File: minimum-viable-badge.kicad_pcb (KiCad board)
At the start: 2 copper layers, 120 x 64 mm, 67 parts, among them J101 EDGE_CONNECTOR, P101 USB, P102 BATTERY, P103 POT_LONG, P104 BUTTON_A, P105 BUTTON_B, P106 POT_SHORT, P107 MECH, P108 MECH, P109 MECH, P301 eInk, Q101 S8050, Q102 S8050, Q201 FDN340P, Q301 IRLML0030TRPBF, SW101 PRGM, SW102 RESET, SW201 ON|OFF, U101 ESP32-WROOM, U102 CP2102, U201 MCP73831, U202 NCP5501

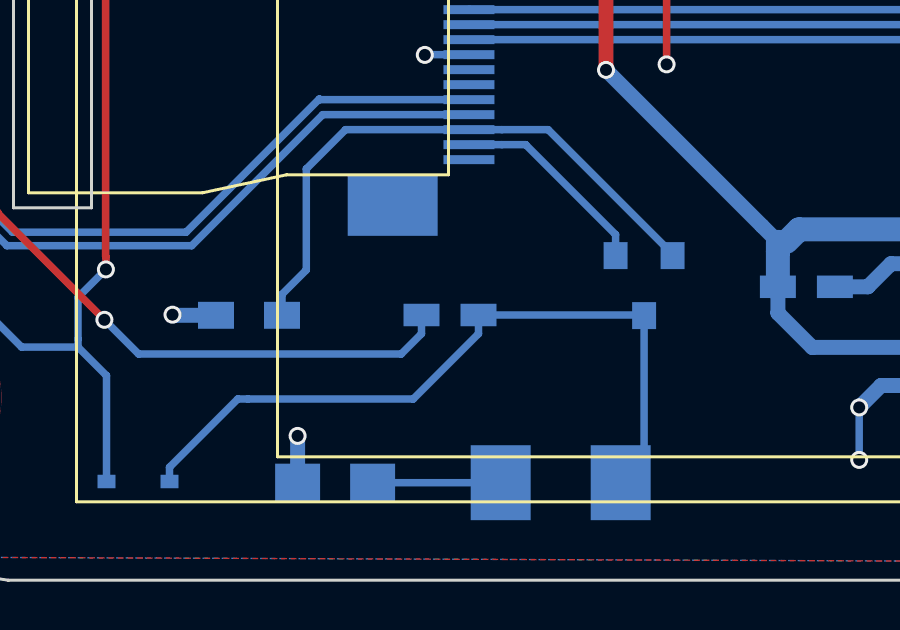
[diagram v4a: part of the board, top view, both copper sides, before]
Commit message: Swap C307 0603->0805
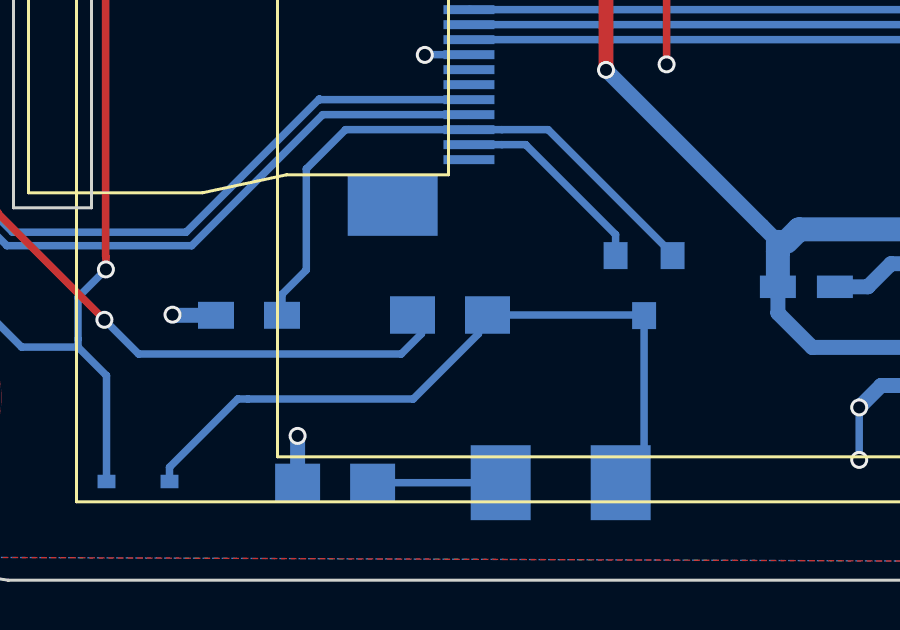
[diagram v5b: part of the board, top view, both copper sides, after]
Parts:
- C306: footprint Capacitors_SMD:C_0603_HandSoldering -> Capacitors_SMD:C_0805_HandSoldering
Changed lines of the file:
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@@
   )
   (setup
-    (last_trace_width 0.5)
+    (last_trace_width 0.25)
     (user_trace_width 0.25)
     (user_trace_width 0.5)
@@
     )
   )
-  (module Capacitors_SMD:C_0603_HandSoldering (layer B.Cu)
-    (at 44.28 73.35483 180)
-    (descr "Capacitor SMD 0603, hand soldering")
-    (tags "capacitor 0603")
-    (attr smd)
-    (fp_text reference C306 (at -0.05 -1.36 180) (layer B.SilkS)
-      (effects (font (size 1 1) (thickness 0.15)) (justify mirror))
-    )
-    (fp_text value "4.7uF 50V" (at 0 1.32 180) (layer B.Fab)
-      (effects (font (size 1 1) (thickness 0.15)) (justify mirror))
-    )
-    (fp_text user %R (at -0.05 -1.38 180) (layer B.Fab)
-      (effects (font (size 1 1) (thickness 0.15)) (justify mirror))
-    )
-    (fp_line (start -0.8 -0.4) (end -0.8 0.4) (layer B.Fab) (width 0.1))
-    (fp_line (start 0.8 -0.4) (end -0.8 -0.4) (layer B.Fab) (width 0.1))
-    (fp_line (start 0.8 0.4) (end 0.8 -0.4) (layer B.Fab) (width 0.1))
-    (fp_line (start -0.8 0.4) (end 0.8 0.4) (layer B.Fab) (width 0.1))
-    (fp_line (start -0.35 0.6) (end 0.35 0.6) (layer B.SilkS) (width 0.12))
-    (fp_line (start 0.35 -0.6) (end -0.35 -0.6) (layer B.SilkS) (width 0.12))
-    (fp_line (start -1.8 0.65) (end 1.8 0.65) (layer B.CrtYd) (width 0.05))
-    (fp_line (start -1.8 0.65) (end -1.8 -0.65) (layer B.CrtYd) (width 0.05))
-    (fp_line (start 1.8 -0.65) (end 1.8 0.65) (layer B.CrtYd) (width 0.05))
-    (fp_line (start 1.8 -0.65) (end -1.8 -0.65) (layer B.CrtYd) (width 0.05))
-    (pad 1 smd rect (at -0.95 0 180) (size 1.2 0.75) (layers B.Cu B.Paste B.Mask)
-      (net 36 "Net-(C306-Pad1)"))
-    (pad 2 smd rect (at 0.95 0 180) (size 1.2 0.75) (layers B.Cu B.Paste B.Mask)
-      (net 37 "Net-(C306-Pad2)"))
-    (model Capacitors_SMD.3dshapes/C_0603.wrl
-      (at (xyz 0 0 0))
-      (scale (xyz 1 1 1))
-      (rotate (xyz 0 0 0))
-    )
-  )
   (module Capacitors_SMD:C_0805_HandSoldering (layer B.Cu)
     (at 40.45 78.93483 180)
@@
       (at (xyz 0 0 0))
       (scale (xyz 1 1 1))
+      (rotate (xyz 0 0 0))
+    )
+  )
+  (module Capacitors_SMD:C_0805_HandSoldering (layer B.Cu)
+    (at 44.28 73.35483 180)
+    (descr "Capacitor SMD 0805, hand soldering")
+    (tags "capacitor 0805")
+    (attr smd)
+    (fp_text reference C306 (at 0 1.75 180) (layer B.SilkS)
+      (effects (font (size 1 1) (thickness 0.15)) (justify mirror))
+    )
+    (fp_text value "4.7uF 50V" (at 0 -1.75 180) (layer B.Fab)
+      (effects (font (size 1 1) (thickness 0.15)) (justify mirror))
+    )
+    (fp_text user %R (at 0 1.75 180) (layer B.Fab)
+      (effects (font (size 1 1) (thickness 0.15)) (justify mirror))
+    )
+    (fp_line (start -1 -0.62) (end -1 0.62) (layer B.Fab) (width 0.1))
+    (fp_line (start 1 -0.62) (end -1 -0.62) (layer B.Fab) (width 0.1))
+    (fp_line (start 1 0.62) (end 1 -0.62) (layer B.Fab) (width 0.1))
+    (fp_line (start -1 0.62) (end 1 0.62) (layer B.Fab) (width 0.1))
+    (fp_line (start 0.5 0.85) (end -0.5 0.85) (layer B.SilkS) (width 0.12))
+    (fp_line (start -0.5 -0.85) (end 0.5 -0.85) (layer B.SilkS) (width 0.12))
+    (fp_line (start -2.25 0.88) (end 2.25 0.88) (layer B.CrtYd) (width 0.05))
+    (fp_line (start -2.25 0.88) (end -2.25 -0.87) (layer B.CrtYd) (width 0.05))
+    (fp_line (start 2.25 -0.87) (end 2.25 0.88) (layer B.CrtYd) (width 0.05))
+    (fp_line (start 2.25 -0.87) (end -2.25 -0.87) (layer B.CrtYd) (width 0.05))
+    (pad 1 smd rect (at -1.25 0 180) (size 1.5 1.25) (layers B.Cu B.Paste B.Mask)
+      (net 36 "Net-(C306-Pad1)"))
+    (pad 2 smd rect (at 1.25 0 180) (size 1.5 1.25) (layers B.Cu B.Paste B.Mask)
+      (net 37 "Net-(C306-Pad2)"))
+    (model Capacitors_SMD.3dshapes/C_0805.wrl
+      (at (xyz 0 0 0))
+      (scale (xyz 1 1 1))

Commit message: Rename power switch SK12D07VG5 -> SK12D07VG3
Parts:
- SW201: footprint libs:SK12D07VG5 -> libs:SK12D07VG3
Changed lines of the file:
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@@
       (net 29 "Net-(C102-Pad1)"))
   )
-  (module libs:SK12D07VG5 (layer B.Cu)
+  (module libs:SK12D07VG3 (layer B.Cu)
     (at 81.68 78.13483)
     (fp_text reference SW201 (at 1.24 1.56) (layer B.SilkS)

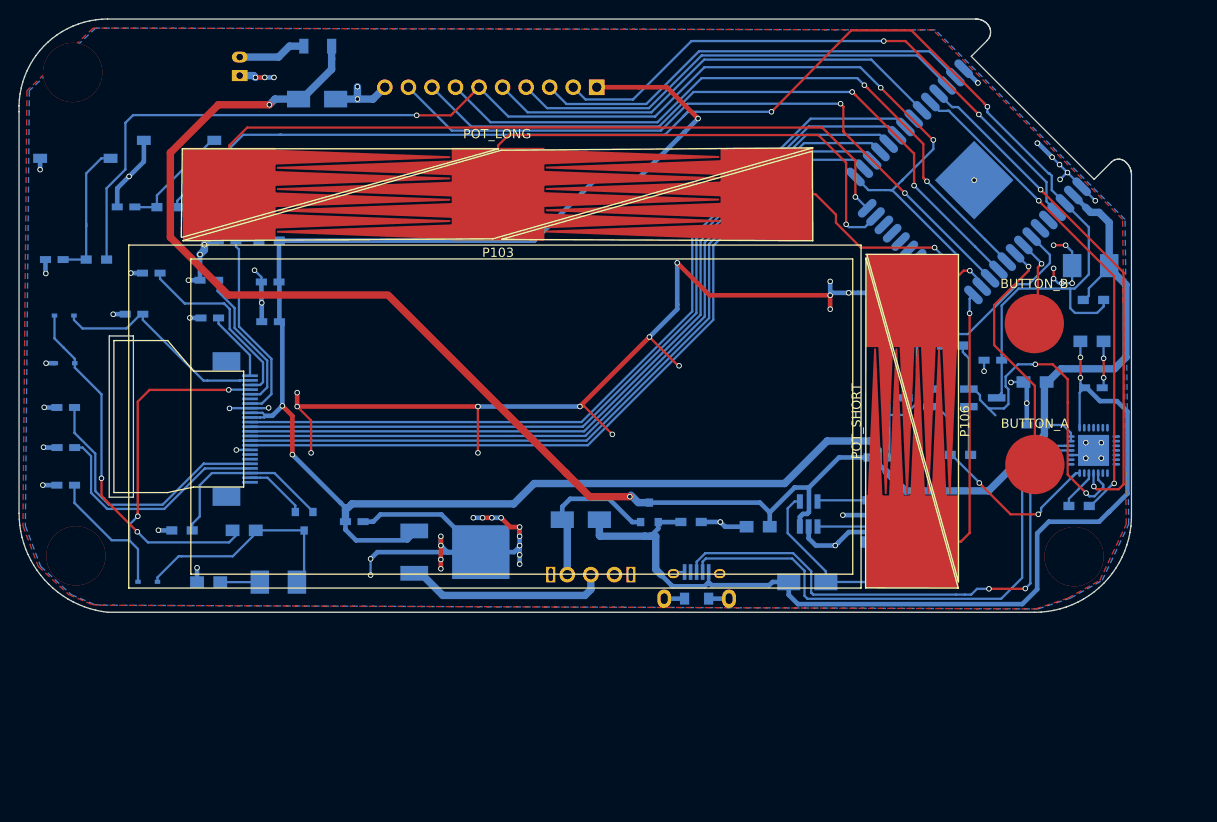
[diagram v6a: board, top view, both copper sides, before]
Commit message: Added edge connector and button silkscreen
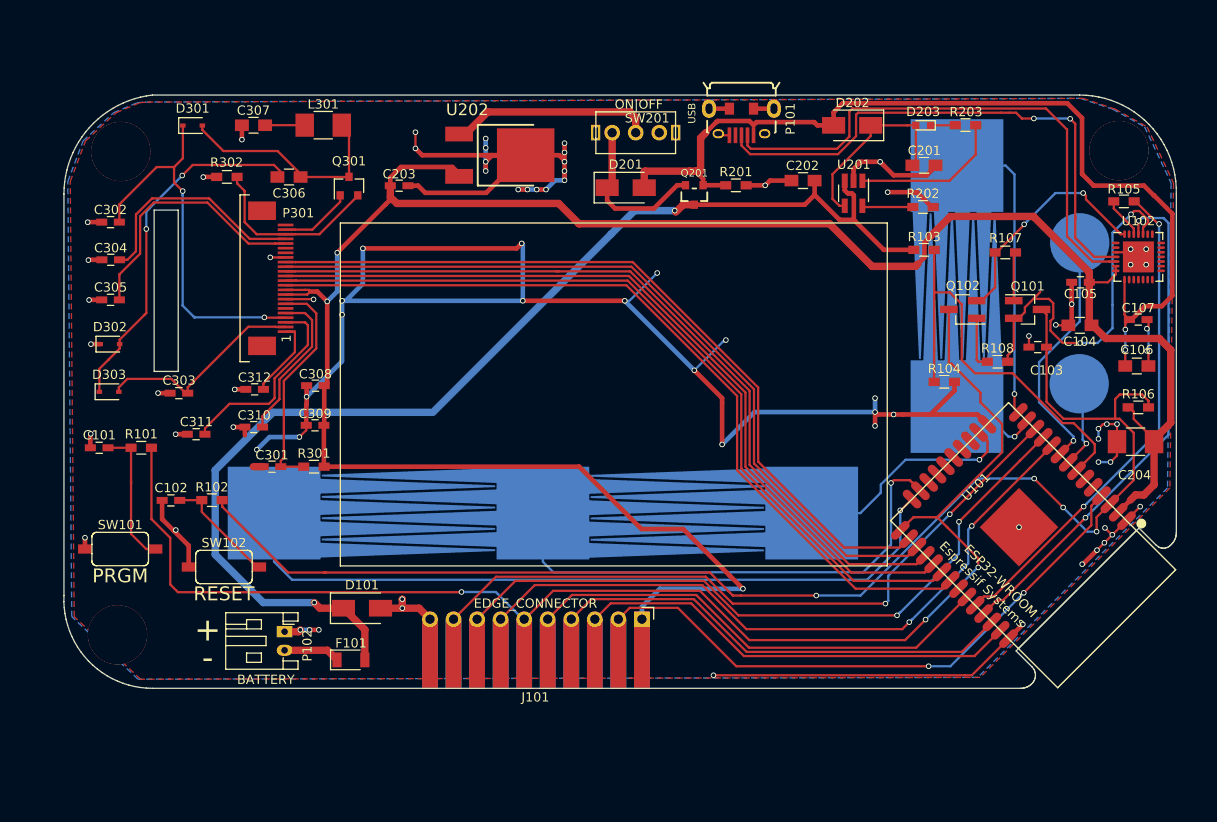
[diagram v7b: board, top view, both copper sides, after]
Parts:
- C101, C102, C103, C104, C105, C106, C107, C201, C202, C203, C204, C301, C302, C303, C304, C305, C306, C307, C308, C309, C310, C311, C312, D101, D201, D202, D203, D301, D302, D303, F101, L301, P101, P102, P107, P108, P109, P301, Q101, Q102, Q201, Q301, R101, R102, R103, R104, R105, R106, R107, R108, R201, R202, R203, R301, R302, SW101, SW102, SW201, U101, U102, U201, U202: moved to F.Cu
- J101: footprint Pin_Headers:Pin_Header_Angled_1x10_Pitch2.54mm -> libs:Edge_Connector_1x10_Pitch2.54mm; moved to F.Cu
- P103, P106: moved to B.Cu
- P104, P105: footprint Mounting_Holes:MountingHole_3.2mm_M3_Pad -> libs:buttons; moved to B.Cu
- moved F101 66.3 mm to (55.8, 87.3)
- moved J101 65.2 mm to (75.7, 90.4), turned to 0 degrees
- moved P108 60.9 mm to (30.6, 84.6)
- moved P102 60.2 mm to (48.6, 84.3), turned to 270 degrees
- moved D101 55.1 mm to (57.0, 81.8)
- moved P101 50.9 mm to (97.9, 29.0), turned to 270 degrees
- moved R203 49.6 mm to (122.1, 29.6)
- moved L301 49.5 mm to (52.8, 29.6)
- moved C307 49.5 mm to (45.3, 29.7)
- moved D203 49.5 mm to (117.5, 29.7)
- moved D202 49.5 mm to (109.9, 29.7)
- moved D301 49.5 mm to (38.7, 29.7)
- moved SW201 47.9 mm to (86.5, 30.5)
- moved SW102 46.3 mm to (42.1, 77.3)
- moved P109 44.1 mm to (138.7, 32.4)
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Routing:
- net GND: track 279.7 -> 343.0 mm, vias 80 -> 79
- net /EN: track 151.0 -> 147.0 mm, vias 2 -> 4
- net +3V3: track 240.5 -> 243.3 mm
- net Net-(F101-Pad1): track 7.41 -> 6.09 mm
- net /EINK_SCLK: track 88.3 -> 89.5 mm
- net /EINK_BUSY: track 84.0 -> 85.2 mm
- net /E-Ink Display/VGH: track 29.1 -> 28.1 mm
- net /EINK_CS: track 87.2 -> 88.2 mm
- net /EINK_RST: track 85.1 -> 86.1 mm
- net /E-Ink Display/VGL: track 25.8 -> 24.8 mm
- net /E-Ink Display/VSH: track 15.9 -> 16.9 mm
- net /E-Ink Display/LCD_VDD: track 23.3 -> 24.3 mm
- net /E-Ink Display/GDR: track 6.83 -> 7.83 mm
- net /E-Ink Display/VSL: track 20.4 -> 21.4 mm
- net /E-Ink Display/VCOM: track 7.64 -> 8.64 mm
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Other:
- outline, holes or cut-outs redrawn

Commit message: Change 3.3V reg to XC6210, enlarge board to move power switch
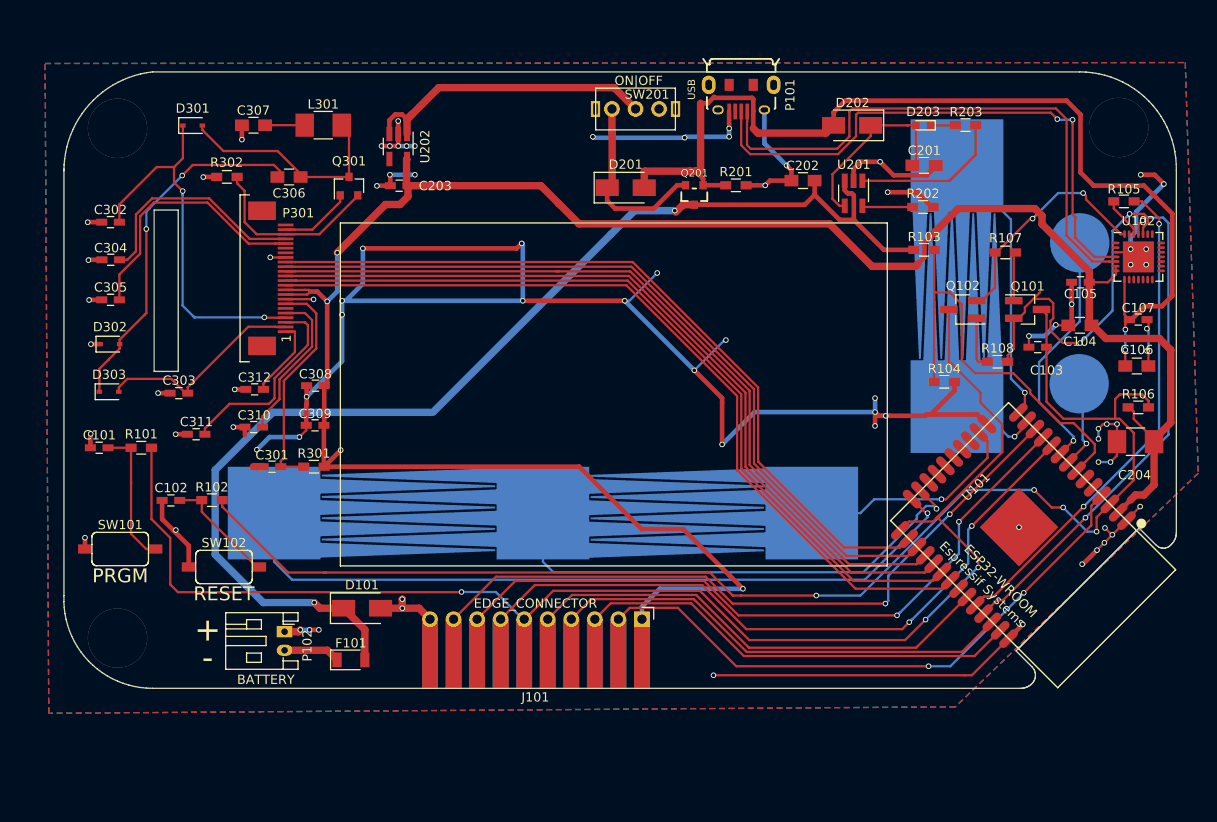
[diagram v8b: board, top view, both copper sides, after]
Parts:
- C101, C102: value 1uF -> 1uF 6.3V
- C201, C202: value 4u7 -> 4.7uF
- C203: value 0.1uF -> 1uF
- C204: value 100uF -> 100uF 10V X5R
- C304, C305, C308, C309, C310, C311, C312: value 1uF -> 1uF 25V
- R103: value 1M -> 1M 1%
- R104: value 100K -> 100K 1%
- R202: value 2K -> 2K 5%
- U202: value NCP5501 -> XC6210A33MR-G; footprint libs:DPAK3.NCP5501 -> TO_SOT_Packages_SMD:SOT-23-5_HandSoldering
- moved U202 11.0 mm to (60.9, 31.9)
- moved P101 2.57 mm to (97.9, 26.4)
- moved SW201 2.56 mm to (86.5, 27.9)
- moved P107 2.52 mm to (30.6, 30.0)
- moved P109 2.50 mm to (138.6, 29.9)
- moved P108 0.35 mm to (30.6, 85.0)
- turned C203 to 180 degrees
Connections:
- U202 pad 2: GND -> Net-(U202-Pad2)
- U202 pad 3: +3V3 -> Net-(SW201-Pad2)
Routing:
- net GND: track 343.0 -> 331.0 mm, vias 79 -> 74
- net Net-(SW201-Pad2): track 21.9 -> 33.3 mm
- net Net-(U202-Pad2): track 0.00 -> 6.30 mm, vias 0 -> 6
- net /USB_VCC: track 103.5 -> 109.3 mm
- net /USB_D-: track 57.9 -> 61.2 mm
- net /USB_D+: track 59.0 -> 61.6 mm
- net /hipster-power/UNREG_V: track 17.4 -> 20.0 mm
- net /IO12: track 87.6 -> 85.2 mm
- net +3V3: track 243.3 -> 240.9 mm, vias 3 -> 4
- net /IO2: track 142.2 -> 143.5 mm
- net /RTS: track 39.9 -> 38.8 mm
- net /EN: track 147.0 -> 146.0 mm
- net /IO15: track 177.7 -> 177.0 mm
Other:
- board size 120 x 64 mm -> 120 x 66.5 mm
